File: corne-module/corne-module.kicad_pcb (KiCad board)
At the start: 2 copper layers, 16.6 x 10.7 mm, 7 parts, among them J1 Battery Connector, J2 nice!view, J3 USB_C_Receptacle_PowerOnly_6P, J4 Battery Wire, U1 ProMicro

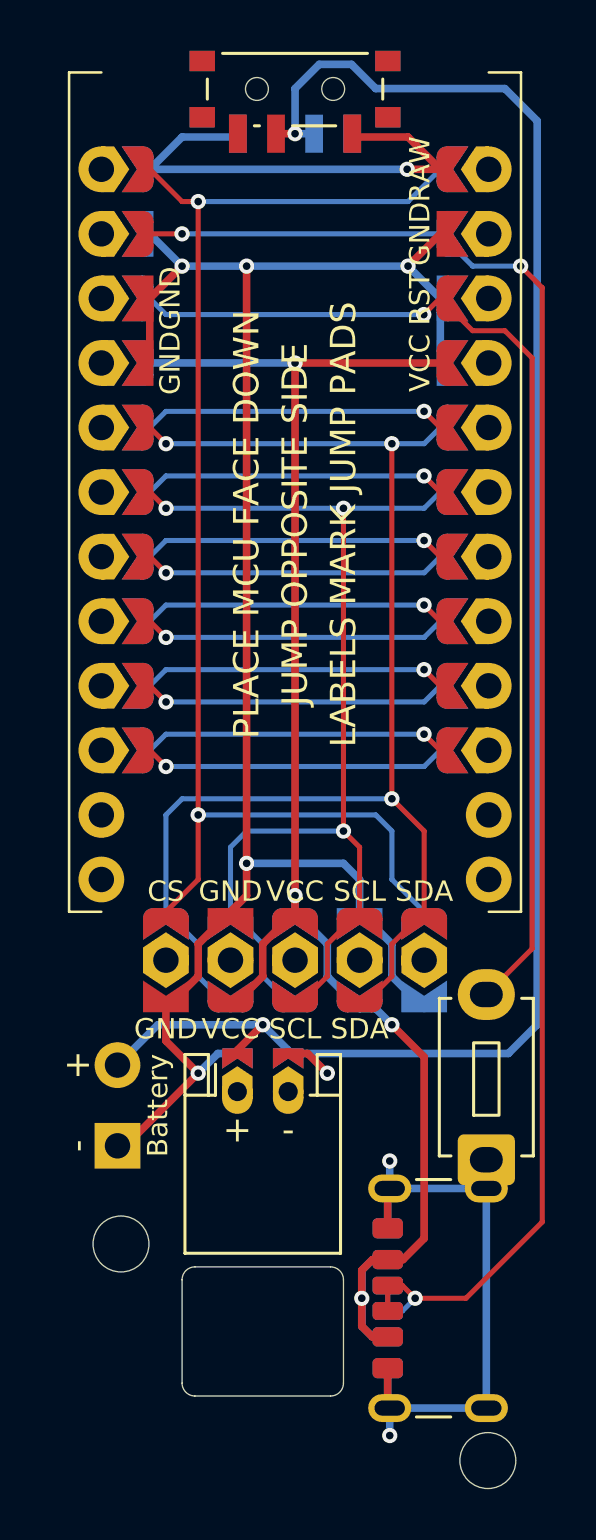
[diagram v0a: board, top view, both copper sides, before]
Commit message: wiring update
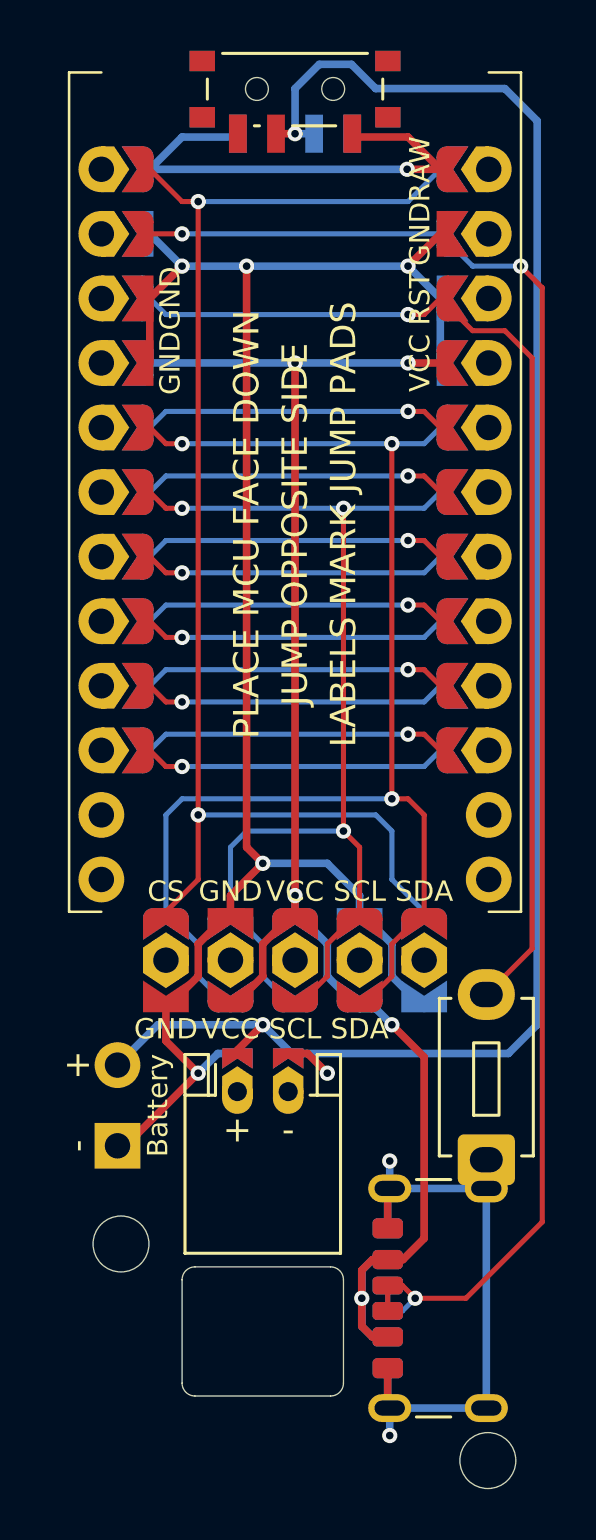
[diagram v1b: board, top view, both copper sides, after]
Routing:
- net VCC: track 64.9 -> 64.8 mm, vias 4 -> 5

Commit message: minor wiring update
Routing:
- net GND: track 99.1 -> 100.1 mm, vias 8 -> 9
- net battery: track 69.4 -> 68.9 mm

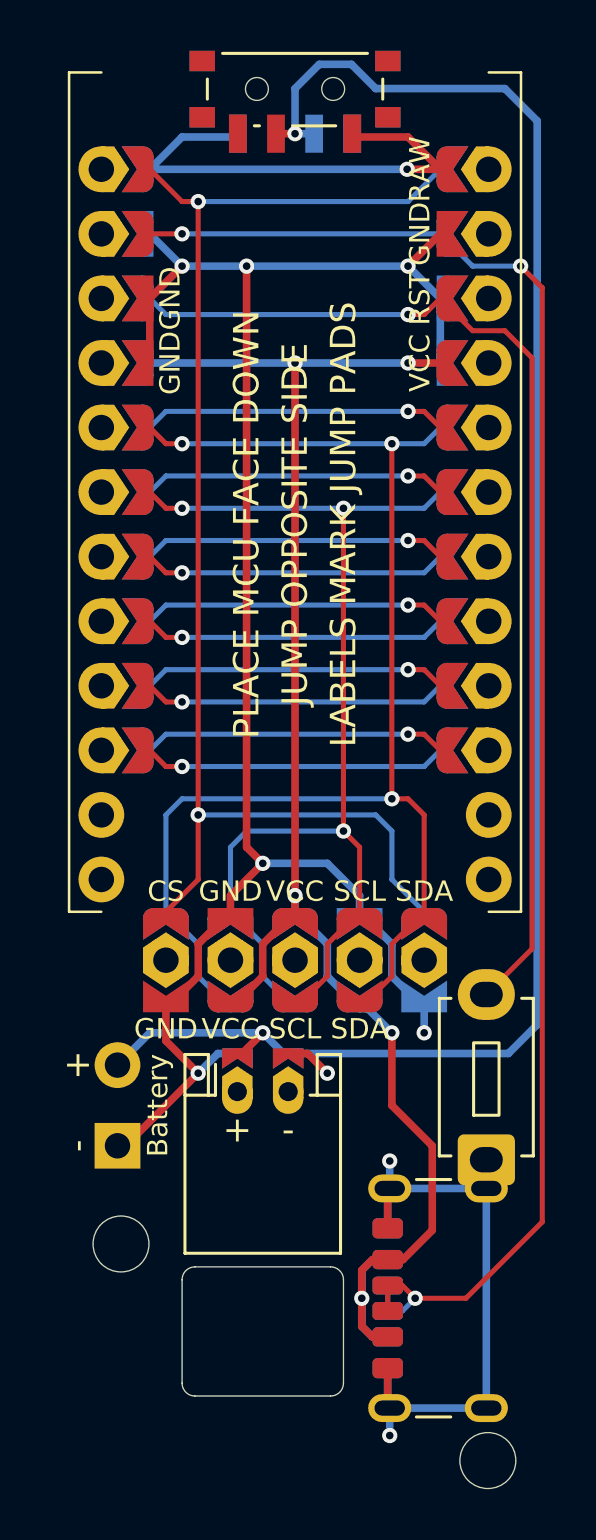
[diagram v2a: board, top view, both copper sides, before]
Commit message: module wiring update
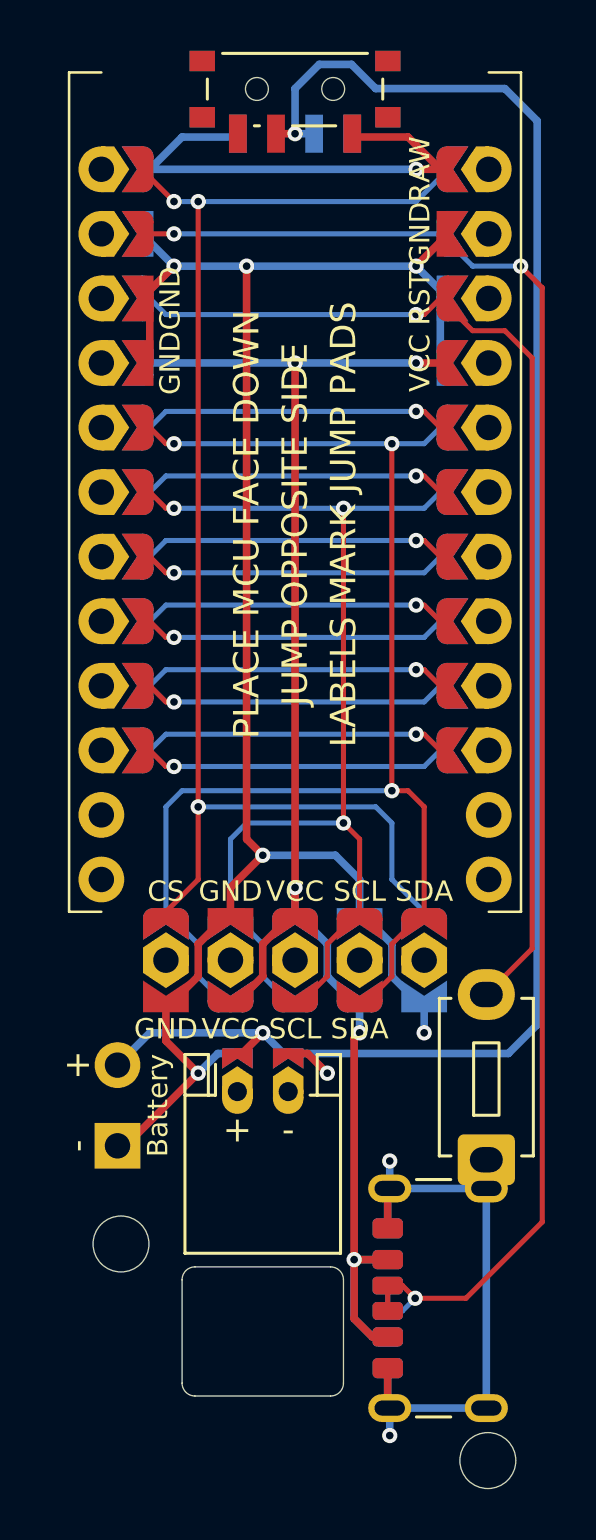
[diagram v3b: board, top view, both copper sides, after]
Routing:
- net VCC: track 64.9 -> 64.2 mm
- net CS: track 52.5 -> 53.2 mm, vias 2 -> 3
- net GND: track 100.1 -> 100.7 mm
